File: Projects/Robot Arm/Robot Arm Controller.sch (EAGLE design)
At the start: 19 parts, among them IC1 U_FTDICHIP_FT232RL, J1 ICSP HEADER, P1 P_USB_MINIUX60A-MB-5ST, U1 U_ATMEGA328P-AU, U2 TPS71550DCKR, U3 UA78M05CDCY, Y1 CSTCE16M0V13

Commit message: Sheet 1 up for review
Sheet 1 for review
library refinements
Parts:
- added C10, C7, C9: 0.1uF, devon:C_CAPACITORC0805
- added C8: 4.7uF, devon:C_CAPACITORC0805
- added LED3, LED4: (no value), devon:D_LEDSML0805
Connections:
- new net N$1: IC1.!RESET
- new net N$11: IC1.3V3OUT
- new net N$12: IC1.TEST
- new net N$13: IC1.CBUS4
- new net N$14: IC1.CBUS3
- new net N$15: IC1.CBUS2
- new net N$2: IC1.OSCI
- new net N$21: IC1.!RI
- new net N$22: IC1.!DCD
- new net N$23: IC1.!DSR
- new net N$24: IC1.!CTS
- new net N$25: IC1.!RTS
- new net N$26: IC1.USBDP, P1.3
- new net N$27: C7.2, IC1.!DTR
- new net N$28: IC1.CBUS0, RN2C.1
- new net N$29: IC1.CBUS1, RN2D.1
- new net N$30: LED3.A, RN2C.2
- new net N$31: LED4.A, RN2D.2
- new net N$32: RN1D.1
- new net N$33: RN1D.2
- new net N$5: IC1.OSCO
- new net N$8: IC1.USBDM, P1.4
- net +5V: now also C10.1, C8.1, C9.1, IC1.VCC, IC1.VCCIO, LED3.C, LED4.C, P1.5
- net GND: now also C10.2, C8.2, C9.2, IC1.GND, IC1.GND@1, IC1.GND@2, IC1.GND@A, P1.1, P1.SHLD
- net RESET: now also C7.1
- net RX: now also IC1.TXD
- net TX: now also IC1.RXD
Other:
- note added: "+5V AUTO SELECT"
- note added: "FTDI USB INTERFACE"
- note added: "ICSP HEADER"
- note added: "MICROCONTROLLER"
- note added: "MICROCONTROLLER MAIN & REF LDOs"
- moved on the sheet: C1, C2, C4, C5, D1, IC1, LED1, P1, R1, RN1A, RN1B, RN1C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

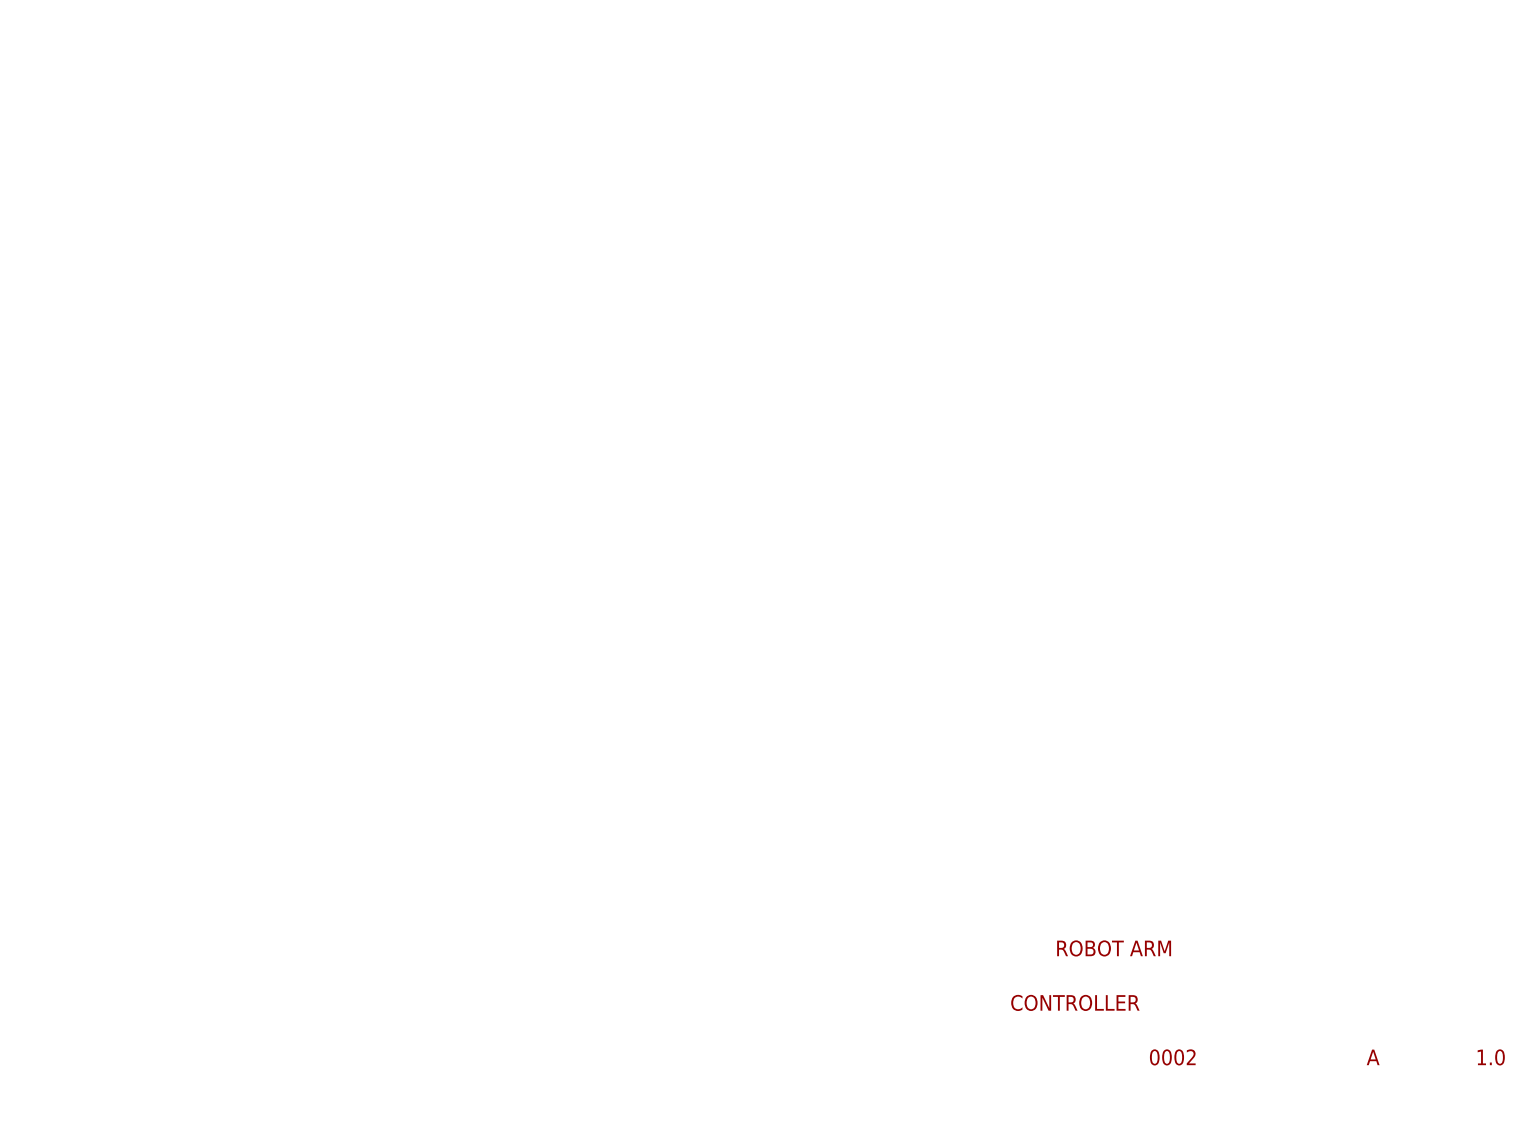
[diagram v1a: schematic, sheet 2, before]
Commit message: FTDI, 5VHP, Opamp, Encoder
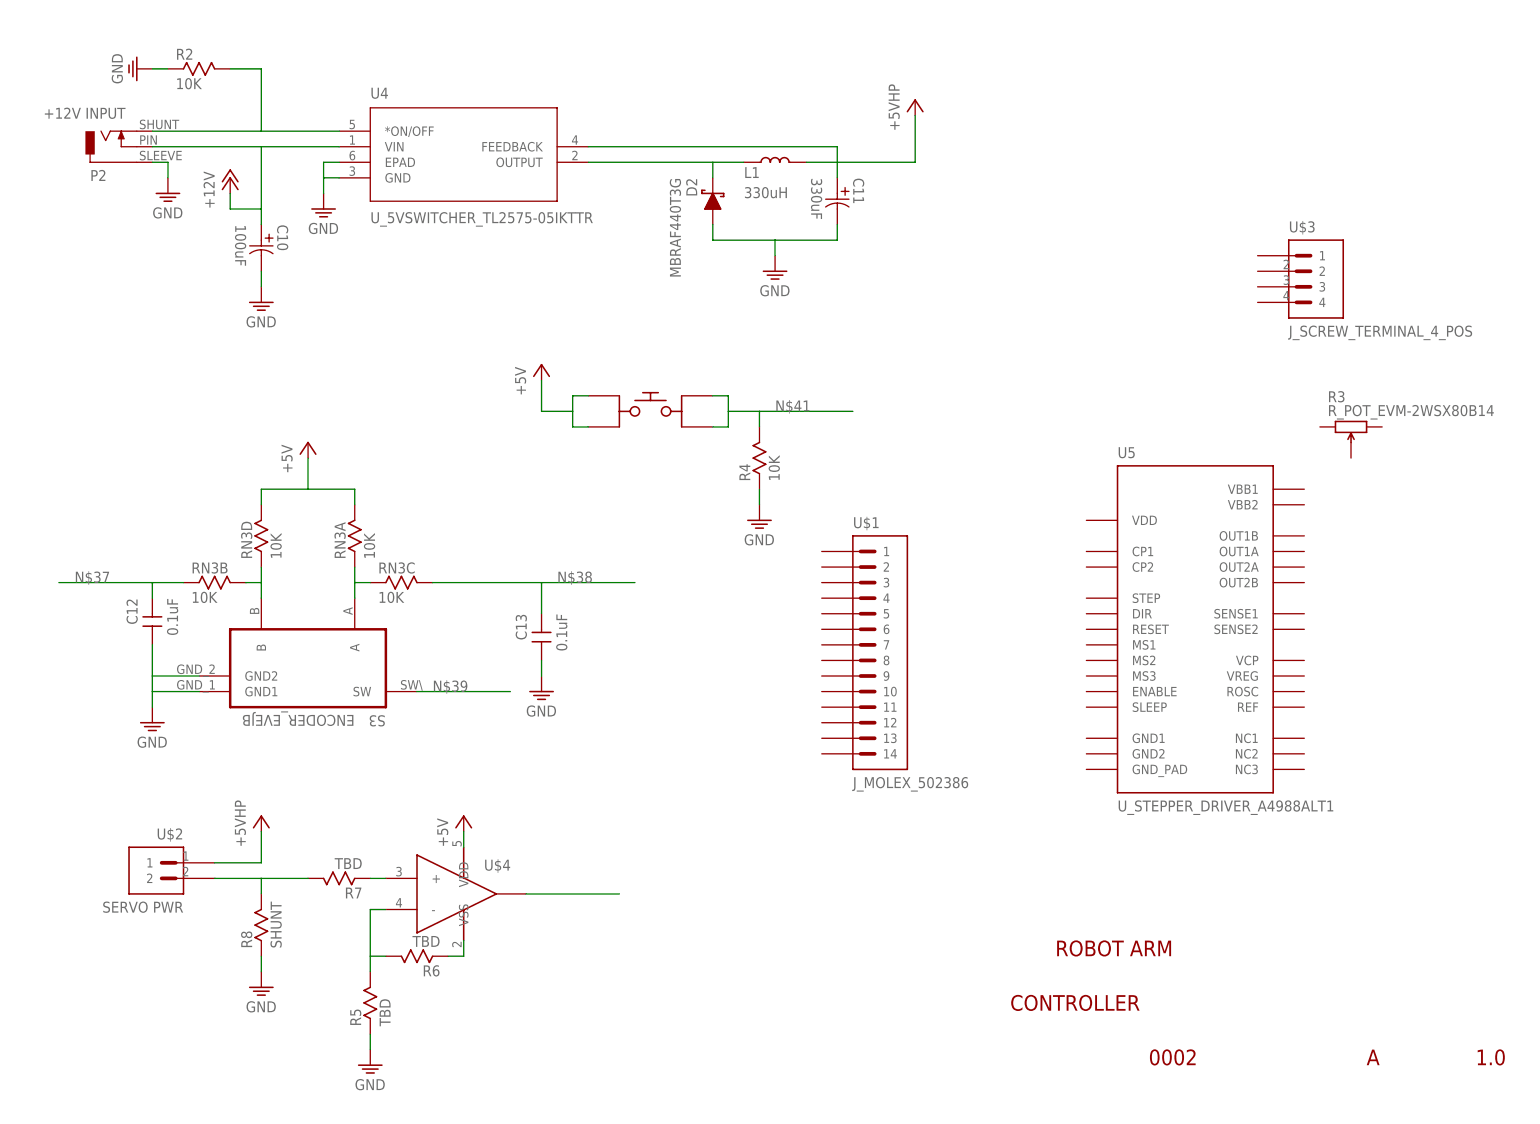
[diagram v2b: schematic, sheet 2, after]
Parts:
- added C11: 330uF, devon:C_CAPACITOR_ALUMINUM_PCAP_SVP_F12
- added C12, C13, C6: 0.1uF, devon:C_CAPACITORC0805
- added D2: MBRAF440T3G, devon:D_SCHOTTKY_MBRAF440T3G
- added L1: 330uH, devon:L_INDUCTOR_CLF12577NI-D
- added P2: +12V INPUT, devon:P_BARREL_2.1MM
- added R2, R4: 10K, devon:R_RESISTOR0805
- added R3: R_POT_EVM-2WSX80B14, devon:R_POT_EVM-2WSX80B14
- added R5, R6, R7: TBD, devon:R_RESISTOR0805
- added R8: SHUNT, devon:R_RESISTOR1206
- added RN3: 10K, devon:R_RESISTOR_NETWORK_EXB-V8V103JV
- added S2: S_BUTTON_TACTILE_PTS645, devon:S_BUTTON_TACTILE_PTS645
- added S3: ENCODER_EVEJB, devon:S_ENCODER_EVEJB
- added U$1: J_MOLEX_502386, devon:J_MOLEX_502386
- added U$2: SERVO PWR, devon:J_SCREW_TERMINAL_2_POS
- added U$3: J_SCREW_TERMINAL_4_POS, devon:J_SCREW_TERMINAL_4_POS
- added U$4: U_OPAMP_MCP6001T-E/OT, devon:U_OPAMP_MCP6001T-E/OT
- added U4: U_5VSWITCHER_TL2575-05IKTTR, devon:U_5VSWITCHER_TL2575-05IKTTR
- added U5: U_STEPPER_DRIVER_A4988ALT1, devon:U_STEPPER_DRIVER_A4988ALT1
- C1, C8: value 4.7uF -> 0.1uF
- C10: value 0.1uF -> 100uF; device devon:C_CAPACITORC0805 -> devon:C_CAPACITOR_ALUMINUM_PCAP_SVP_F12
- C3, C9: value 0.1uF -> 4.7uF
- RN1: value 10K -> 330K
- RN2: value 330K -> 10K
- U1: value U_ATMEGA328P-AU -> UA78M05CDCY; device devon:U_ATMEGA328P-AU -> devon:U_5VLDO_UA78M05CDCY
- U3: value UA78M05CDCY -> U_ATMEGA328P-AU; device devon:U_5VLDO_UA78M05CDCY -> devon:U_ATMEGA328P-AU
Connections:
- new net +12V: C1.1, C10.11, C4.1, P2.PIN, U1.VIN, U2.VIN, U4.VIN
- new net N$34: RN3B.2, RN3D.1, S3.B
- new net N$35: P2.SHUNT, R2.2, U4.*ON/OFF
- new net N$36: RN3A.1, RN3C.1, S3.A
- new net N$37: C12.2, RN3B.1
- new net N$38: C13.2, RN3C.2
- new net N$39: S3.SW
- new net N$41: R4.2, S2.3, S2.4
- new net N$42: R6.1, U$4.VSS
- new net N$43: R7.1, U$4.+
- new net N$44: R5.2, R6.2, U$4.-
- new net N$45: R7.2, R8.2, U$2.2
- new net N$49: U$4.VOUT
- net +5V: now also C11.11, C3.1, C5.1, C6.1, L1.2, RN1B.2, RN2A.2, RN3A.2, RN3D.2, S2.1, S2.2, U$2.1, U$4.VDD, U1.VOUT, U3.AVCC, U3.VCC1, U3.VCC2, U4.FEEDBACK; no longer C1.1, C10.1, C8.1, RN1A.2, RN2B.2, U1.AVCC, U1.VCC1, U1.VCC2, U3.VOUT
- net A0: now also U3.PC0(ADC0); no longer U1.PC0(ADC0)
- net A1: now also U3.PC1(ADC1); no longer U1.PC1(ADC1)
- net A2: now also U3.PC2(ADC2); no longer U1.PC2(ADC2)
- net A3: now also U3.PC3(ADC3); no longer U1.PC3(ADC3)
- net A4: now also U3.PC4(ADC4); no longer U1.PC4(ADC4)
- net A5: now also U3.PC5(ADC5); no longer U1.PC5(ADC5)
- net A6: now also U3.ADC6; no longer U1.ADC6
- net A7: now also U3.ADC7; no longer U1.ADC7
- net D10: now also U3.PB2; no longer U1.PB2
- net D11/MOSI: now also U3.PB3; no longer U1.PB3
- net D12/MISO: now also U3.PB4; no longer U1.PB4
- net D13/SCK: now also RN1A.2, U3.PB5; no longer RN2A.2, U1.PB5
- net D2: now also U3.PD2; no longer U1.PD2
- net D3: now also U3.PD3; no longer U1.PD3
- net D4: now also U3.PD4; no longer U1.PD4
- net D5: now also U3.PD5; no longer U1.PD5
- net D6: now also U3.PD6; no longer U1.PD6
- net D7: now also U3.PD7; no longer U1.PD7
- net D8: now also U3.PB0; no longer U1.PB0
- net D9: now also U3.PB1; no longer U1.PB1
- net GND: now also C10.22, C11.22, C12.1, C6.2, C7.2, D2.A, P2.SLEEVE, R2.1, R4.1, R5.1, R8.1, S3.GND1, S3.GND2, U1.GND1, U1.GND2, U3.GND, U3.GND_2, U3.GND_3, U4.EPAD, U4.GND; no longer C10.2, C8.2, U1.GND, U1.GND_2, U1.GND_3, U3.GND1, U3.GND2
- net N$16: now also U3.PB6(XTAL1); no longer U1.PB6(XTAL1)
- net N$17: now also LED2.A, RN1A.1; no longer LED1.A, RN2A.1
- net N$19: now also D2.C, L1.1, U4.OUTPUT; no longer C3.1, C5.1, U2.VIN, U3.VIN
- net N$20: now also RN2B.1, U3.PD0; no longer RN1B.1, U1.PD0
- net N$27: now also C8.2; no longer C7.2
- net N$28: now also RN1C.1; no longer RN2C.1
- net N$29: now also RN1D.1; no longer RN2D.1
- net N$3: now also LED1.A, RN1B.1; no longer LED2.A, RN2B.1
- net N$30: now also RN1C.2; no longer RN2C.2
- net N$31: now also RN1D.2; no longer RN2D.2
- net N$32: now also RN2D.1; no longer RN1D.1
- net N$33: now also RN2D.2; no longer RN1D.2
- net N$4: now also U3.PB7(XTAL2); no longer U1.PB7(XTAL2)
- net N$6: now also C7.1, U3.AREF; no longer C4.1, U1.AREF
- net N$9: now also RN2C.1, U3.PD1; no longer RN1C.1, U1.PD1
- net RESET: now also C8.1, RN2A.1, U3.PC6(RESET); no longer C7.1, RN1A.1, U1.PC6(RESET)
- net RX: now also RN2B.2; no longer RN1B.2
- net TX: now also RN2C.2; no longer RN1C.2
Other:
- moved on the sheet: C1, C2, C3, C4, C5, C7, C8, C9, LED1, LED2, RN1A, RN1B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

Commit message: Full schematic up for review
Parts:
- removed U$1: J_MOLEX_502386, devon:J_MOLEX_502386
- removed U$2: SERVO PWR, devon:J_SCREW_TERMINAL_2_POS
- removed U$3: J_SCREW_TERMINAL_4_POS, devon:J_SCREW_TERMINAL_4_POS
- removed U$4: U_OPAMP_MCP6001T-E/OT, devon:U_OPAMP_MCP6001T-E/OT
- added C14: 0.22uF, devon:C_CAPACITORC0805
- added C15: 100uF, devon:C_CAPACITOR_ALUMINUM_PCAP_SVP_F12
- added C16: 4.7uF, devon:C_CAPACITORC1206
- added C17: 330uF, devon:C_CAPACITOR_ALUMINUM_PCAP_SVP_F12
- added C18, C19, C20: 0.1uF, devon:C_CAPACITORC0805
- added J2: SERVO PWR, devon:J_SCREW_TERMINAL_2_POS
- added J3: STEPPER, devon:J_SCREW_TERMINAL_4_POS
- added J4: J_MOLEX_502386, devon:J_MOLEX_502386
- added R10, R11, R12: TBD, devon:R_RESISTOR0805
- added R13, R14: 0.05, devon:R_RESISTOR1206
- added R15, R17: 10K, devon:R_RESISTOR0805
- added R16: TBD, devon:R_POT_EVM-2WSX80B14
- added R9: SHUNT, devon:R_RESISTOR1206
- added U6: U_OPAMP_MCP6001T-E/OT, devon:U_OPAMP_MCP6001T-E/OT
- C10: value 100uF -> 0.1uF; device devon:C_CAPACITOR_ALUMINUM_PCAP_SVP_F12 -> devon:C_CAPACITORC0805
- C11: value 330uF -> 100uF
- C12: value 0.1uF -> 0.22uF
- R2: value 10K -> 0
- R3: value R_POT_EVM-2WSX80B14 -> 10K; device devon:R_POT_EVM-2WSX80B14 -> devon:R_RESISTOR0805
- R4: value 10K -> 100K
- R5: value TBD -> 10K
- R6, R7: value TBD -> 0
- R8: value SHUNT -> 0; device devon:R_RESISTOR1206 -> devon:R_RESISTOR0805
- S2: value S_BUTTON_TACTILE_PTS645 -> ENCODER_EVEJB; device devon:S_BUTTON_TACTILE_PTS645 -> devon:S_ENCODER_EVEJB
- S3: value ENCODER_EVEJB -> S_BUTTON_TACTILE_PTS645; device devon:S_ENCODER_EVEJB -> devon:S_BUTTON_TACTILE_PTS645
- U5: value U_STEPPER_DRIVER_A4988ALT1 -> A4988ALT1
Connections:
- new net AUX: J4.13
- new net BASE_LED: J4.7
- new net DIR: U5.DIR
- new net ELBOW_PWM: J4.6
- new net ENABLE: U5.ENABLE
- new net FOREARM_LED: J4.3
- new net GRIP_LED: J4.1
- new net GRIP_PWM: J4.2
- new net HALL_SIGNAL: J4.10
- new net N$40: J3.1, U5.OUT1B
- new net N$46: J3.2, U5.OUT1A
- new net N$47: J3.3, U5.OUT2A
- new net N$48: J3.4, U5.OUT2B
- new net N$50: C14.1, U5.VREG
- new net N$51: R13.2, U5.SENSE2
- new net N$52: R15.1, R16.1
- new net N$53: R14.2, U5.SENSE1
- new net N$54: R16.2, U5.REF
- new net N$55: U5.NC1
- new net N$56: U5.NC2
- new net N$57: U5.NC3
- new net N$58: C13.2, U5.VCP
- new net N$59: C10.2, U5.CP2
- new net N$60: C10.1, U5.CP1
- new net N$61: R7.2, U5.MS2
- new net N$62: R6.2, U5.MS1
- new net N$63: R8.2, U5.MS3
- new net N$64: R4.1, U5.RESET, U5.SLEEP
- new net N$65: R2.1, R3.2, U5.ROSC
- new net SHOULDER_PWM1: J4.8
- new net SHOULDER_PWM2: J4.9
- new net STEP: U5.STEP
- new net UPPER_LED: J4.5
- new net WRIST_LED: J4.4
- net +12V: now also C11.11, C13.1, C15.11, C16.2, C18.1, U5.VBB1, U5.VBB2; no longer C10.11
- net +5V: now also C12.1, C17.11, J2.1, J4.11, R15.2, R2.2, R4.2, R6.1, R7.1, R8.1, S3.1, S3.2, U5.VDD, U6.VDD; no longer C11.11, S2.1, S2.2, U$2.1, U$4.VDD
- net GND: now also C12.2, C14.2, C15.22, C16.1, C17.22, C18.2, C19.1, C20.1, J4.12, R11.1, R13.1, R14.1, R16.3, R17.1, R3.1, R9.1, S2.GND1, S2.GND2, U5.GND1, U5.GND2, U5.GND_PAD; no longer C10.22, C12.1, R2.1, R4.1, R8.1, S3.GND1, S3.GND2
- net N$34: now also S2.B; no longer S3.B
- net N$35: now also R5.2; no longer R2.2
- net N$36: now also S2.A; no longer S3.A
- net N$37: now also C19.2; no longer C12.2
- net N$38: now also C20.2; no longer C13.2
- net N$39: now also S2.SW; no longer S3.SW
- net N$41: now also R17.2, S3.3, S3.4; no longer R4.2, S2.3, S2.4
- net N$42: now also R12.1, U6.VSS; no longer R6.1, U$4.VSS
- net N$43: now also R10.1, U6.+; no longer R7.1, U$4.+
- net N$44: now also R11.2, R12.2, U6.-; no longer R5.2, R6.2, U$4.-
- net N$45: now also J2.2, R10.2, R9.2; no longer R7.2, R8.2, U$2.2
- net N$49: now also U6.VOUT; no longer U$4.VOUT
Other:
- note added: "+5V HIGH POWER SWITCHER"
- note added: "BREAKOUT HEADER"
- note added: "ENCODER"
- note added: "MICROSTEPPING CONFIG: SEE DATASHEET"
- note added: "POPULATE R17 TO ENABLE TBD"
- note added: "STEPPER CONTROLLER"
- note added: "USER INPUT"
- moved on the sheet: C11, C12, C13, D2, L1, P2, R2, R4, R5, R6, R7, R8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
